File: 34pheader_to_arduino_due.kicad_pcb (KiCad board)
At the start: 2 copper layers, 29 x 59 mm, 7 parts, among them J1 Conn_02x17_Odd_Even, J2 Conn_02x17_Odd_Even, J3 Conn_01x02_Pin, J4 Conn_01x02_Pin, J5 Conn_01x02_Pin

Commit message: Add WayWayWay text to indicate the project number should be on the back silkscreen
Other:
- board text added: "WayWayWay"
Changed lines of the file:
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@@
   (gr_rect (start 206 19) (end 235 78)
     (stroke (width 0.05) (type default)) (fill none) (layer "Edge.Cuts"))
+  (gr_text "WayWayWay" (at 209.55 25.4 90) (layer "B.SilkS")
+    (effects (font (size 1 1) (thickness 0.15)) (justify left bottom mirror))
+  )
   (segment (start 231.14 63.5) (end 229.87 64.77) (width 0.25) (layer "B.Cu") (net 1))
   (segment (start 226.06 64.77) (end 218.44 72.39) (width 0.25) (layer "B.Cu") (net 1))

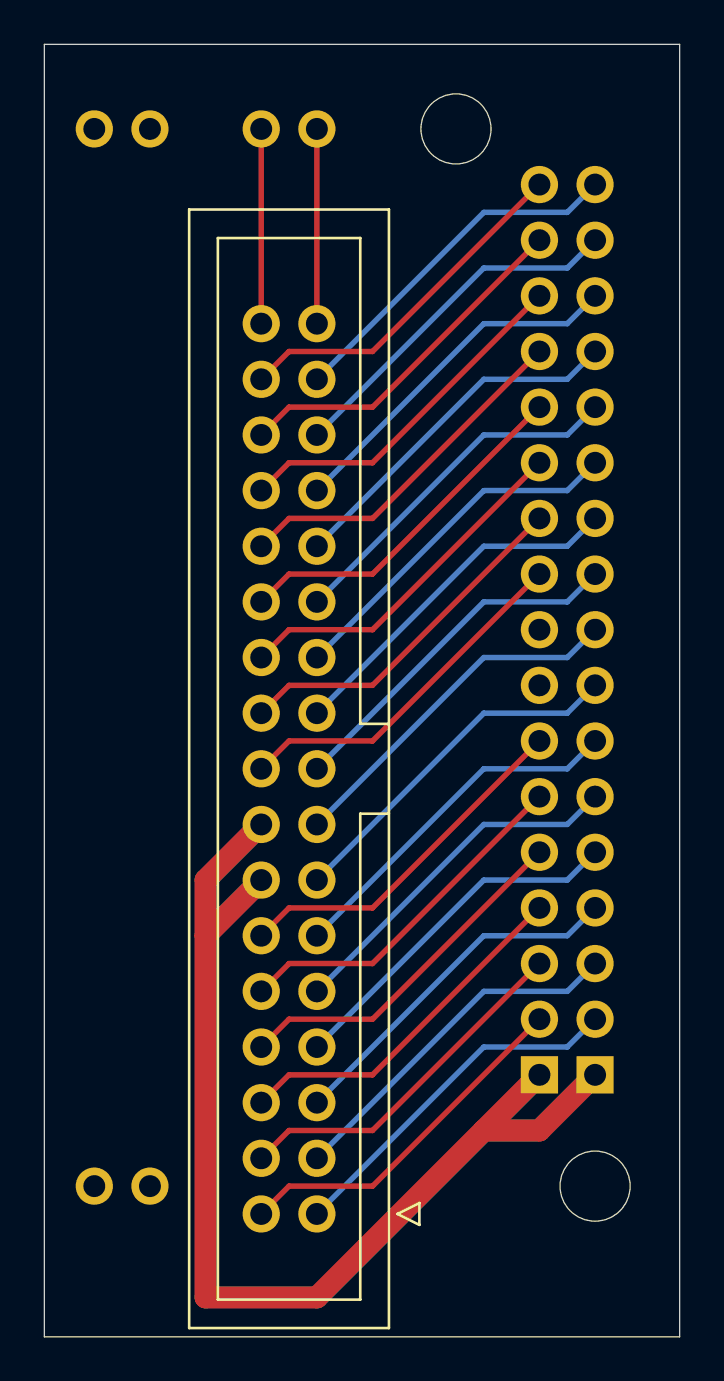
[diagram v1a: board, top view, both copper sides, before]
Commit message: Add pin numbers on silk screen layer
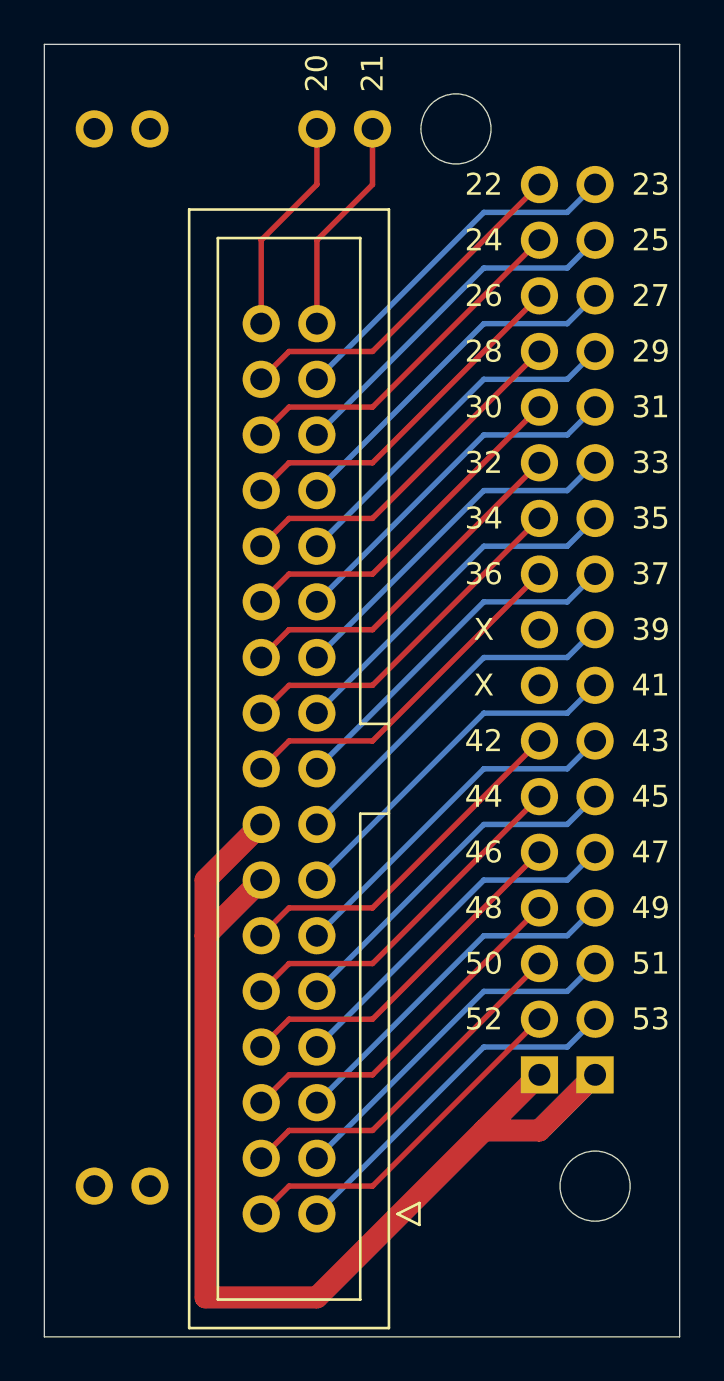
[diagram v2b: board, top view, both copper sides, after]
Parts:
- moved J3 2.54 mm to (221.0, 22.9)
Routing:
- net Net-(J1-Pin_34): track 8.89 -> 9.94 mm
- net Net-(J1-Pin_33): track 8.89 -> 9.94 mm
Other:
- board text added: "20"
- board text added: "21"
- board text added: "22"
- board text added: "23"
- board text added: "24"
- board text added: "25"
- board text added: "26"
- board text added: "27"
- board text added: "28"
- board text added: "29"
- board text added: "30"
- board text added: "31"
- board text added: "32"
- board text added: "33"
- board text added: "34"
- board text added: "35"
- board text added: "36"
- board text added: "37"
- board text added: "39"
- board text added: "41"
- board text added: "42"
- board text added: "43"
- board text added: "44"
- board text added: "45"
- board text added: "46"
- board text added: "47"
- board text added: "48"
- board text added: "49"
- board text added: "50"
- board text added: "51"
- board text added: "52"
- board text added: "53"
- board text added: "X"
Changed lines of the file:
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@@
   )
   (footprint "Connector_PinHeader_2.54mm:PinHeader_1x02_P2.54mm_Vertical" (layer "B.Cu")
-    (at 218.44 22.86 90)
+    (at 220.98 22.86 90)
     (descr "Through hole straight pin header, 1x02, 2.54mm pitch, single row")
     (tags "Through hole pin header THT 1x02 2.54mm single row")
@@
   (gr_text "WayWayWay" (at 209.55 25.4 90) (layer "B.SilkS")
     (effects (font (size 1 1) (thickness 0.15)) (justify left bottom mirror))
+  )
+  (gr_text "31" (at 233.68 35.56) (layer "F.SilkS")
+    (effects (font (size 1 1) (thickness 0.15)))
+  )
+  (gr_text "X" (at 226.06 45.72) (layer "F.SilkS")
+    (effects (font (size 1 1) (thickness 0.15)))
+  )
+  (gr_text "48" (at 226.06 58.42) (layer "F.SilkS")
+    (effects (font (size 1 1) (thickness 0.15)))
+  )
+  (gr_text "45" (at 233.68 53.34) (layer "F.SilkS")
+    (effects (font (size 1 1) (thickness 0.15)))
+  )
+  (gr_text "50" (at 226.06 60.96) (layer "F.SilkS")
+    (effects (font (size 1 1) (thickness 0.15)))
+  )
+  (gr_text "42" (at 226.06 50.8) (layer "F.SilkS")
+    (effects (font (size 1 1) (thickness 0.15)))
+  )
+  (gr_text "49" (at 233.68 58.42) (layer "F.SilkS")
+    (effects (font (size 1 1) (thickness 0.15)))
+  )
+  (gr_text "36" (at 226.06 43.18) (layer "F.SilkS")
+    (effects (font (size 1 1) (thickness 0.15)))
+  )
+  (gr_text "24" (at 226.06 27.94) (layer "F.SilkS")
+    (effects (font (size 1 1) (thickness 0.15)))
+  )
+  (gr_text "32" (at 226.06 38.1) (layer "F.SilkS")
+    (effects (font (size 1 1) (thickness 0.15)))
+  )
+  (gr_text "20" (at 218.44 20.32 90) (layer "F.SilkS")
+    (effects (font (size 1 1) (thickness 0.15)))
+  )
+  (gr_text "51" (at 233.68 60.96) (layer "F.SilkS")
+    (effects (font (size 1 1) (thickness 0.15)))
+  )
+  (gr_text "29" (at 233.68 33.02) (layer "F.SilkS")
+    (effects (font (size 1 1) (thickness 0.15)))
+  )
+  (gr_text "52" (at 226.06 63.5) (layer "F.SilkS")
+    (effects (font (size 1 1) (thickness 0.15)))
+  )
+  (gr_text "23" (at 233.68 25.4) (layer "F.SilkS")
+    (effects (font (size 1 1) (thickness 0.15)))
+  )
+  (gr_text "34" (at 226.06 40.64) (layer "F.SilkS")
+    (effects (font (size 1 1) (thickness 0.15)))
+  )
+  (gr_text "33" (at 233.68 38.1) (layer "F.SilkS")
+    (effects (font (size 1 1) (thickness 0.15)))
+  )
+  (gr_text "39" (at 233.68 45.72) (layer "F.SilkS")
+    (effects (font (size 1 1) (thickness 0.15)))
+  )
+  (gr_text "37" (at 233.68 43.18) (layer "F.SilkS")
+    (effects (font (size 1 1) (thickness 0.15)))
+  )
+  (gr_text "30" (at 226.06 35.56) (layer "F.SilkS")
+    (effects (font (size 1 1) (thickness 0.15)))
+  )
+  (gr_text "53" (at 233.68 63.5) (layer "F.SilkS")
+    (effects (font (size 1 1) (thickness 0.15)))
+  )
+  (gr_text "25" (at 233.68 27.94) (layer "F.SilkS")
+    (effects (font (size 1 1) (thickness 0.15)))
+  )
+  (gr_text "43" (at 233.68 50.8) (layer "F.SilkS")
+    (effects (font (size 1 1) (thickness 0.15)))
+  )
+  (gr_text "41" (at 233.68 48.26) (layer "F.SilkS")
+    (effects (font (size 1 1) (thickness 0.15)))
+  )
+  (gr_text "26" (at 226.06 30.48) (layer "F.SilkS")
+    (effects (font (size 1 1) (thickness 0.15)))
+  )
+  (gr_text "27" (at 233.68 30.48) (layer "F.SilkS")
+    (effects (font (size 1 1) (thickness 0.15)))
+  )
+  (gr_text "35" (at 233.68 40.64) (layer "F.SilkS")
+    (effects (font (size 1 1) (thickness 0.15)))
+  )
+  (gr_text "28" (at 226.06 33.02) (layer "F.SilkS")
+    (effects (font (size 1 1) (thickness 0.15)))
+  )
+  (gr_text "22" (at 226.06 25.4) (layer "F.SilkS")
+    (effects (font (size 1 1) (thickness 0.15)))
+  )
+  (gr_text "47" (at 233.68 55.88) (layer "F.SilkS")
+    (effects (font (size 1 1) (thickness 0.15)))
+  )
+  (gr_text "44" (at 226.06 53.34) (layer "F.SilkS")
+    (effects (font (size 1 1) (thickness 0.15)))
+  )
+  (gr_text "46" (at 226.06 55.88) (layer "F.SilkS")
+    (effects (font (size 1 1) (thickness 0.15)))
+  )
+  (gr_text "X" (at 226.06 48.26) (layer "F.SilkS")
+    (effects (font (size 1 1) (thickness 0.15)))
+  )
+  (gr_text "21" (at 220.98 20.32 90) (layer "F.SilkS")
+    (effects (font (size 1 1) (thickness 0.15)))
   )
   (segment (start 231.14 63.5) (end 229.87 64.77) (width 0.25) (layer "B.Cu") (net 1))
@@
   (segment (start 220.98 33.02) (end 228.6 25.4) (width 0.25) (layer "F.Cu") (net 30))
   (segment (start 217.17 33.02) (end 220.98 33.02) (width 0.25) (layer "F.Cu") (net 30))
-  (segment (start 218.44 31.75) (end 218.44 22.86) (width 0.25) (layer "F.Cu") (net 31))
-  (segment (start 215.9 31.75) (end 215.9 22.86) (width 0.25) (layer "F.Cu") (net 32))
+  (segment (start 220.98 25.4) (end 220.98 22.86) (width 0.25) (layer "F.Cu") (net 31))
+  (segment (start 218.44 27.94) (end 220.98 25.4) (width 0.25) (layer "F.Cu") (net 31))
+  (segment (start 218.44 31.75) (end 218.44 27.94) (width 0.25) (layer "F.Cu") (net 31))
+  (segment (start 215.9 27.94) (end 215.9 31.75) (width 0.25) (layer "F.Cu") (net 32))
+  (segment (start 218.44 22.86) (end 218.44 25.4) (width 0.25) (layer "F.Cu") (net 32))
+  (segment (start 218.44 25.4) (end 215.9 27.94) (width 0.25) (layer "F.Cu") (net 32))
   (segment (start 218.44 76.2) (end 213.36 76.2) (width 1) (layer "F.Cu") (net 39))
   (segment (start 213.36 59.69) (end 213.36 57.15) (width 1) (layer "F.Cu") (net 39))

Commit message: Add GND label
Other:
- board text added: "GND"
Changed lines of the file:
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@@
     )
   )
+  (gr_rect (start 227.33 64.77) (end 232.41 67.31)
+    (stroke (width 0.12) (type default)) (fill none) (layer "F.SilkS"))
   (gr_rect (start 206 19) (end 235 78)
     (stroke (width 0.05) (type default)) (fill none) (layer "Edge.Cuts"))
@@
     (effects (font (size 1 1) (thickness 0.15)))
   )
+  (gr_text "GND" (at 225.425 66.04) (layer "F.SilkS")
+    (effects (font (size 1 1) (thickness 0.15)))
+  )

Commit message: Ensure pinout is correct
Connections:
- J1 pad 16: Net-(J1-Pin_14) -> Net-(J1-Pin_16)
- J1 pad 22: Net-(J1-Pin_22) -> Net-(J1-Pin_20)
- J2 pad 1: Net-(J1-Pin_14) -> Net-(J1-Pin_20)
- J2 pad 16: unconnected-(J2-Pin_16-Pad16) -> Net-(J1-Pin_14)
- J2 pad 18: unconnected-(J2-Pin_18-Pad18) -> Net-(J1-Pin_16)
- J2 pad 2: Net-(J1-Pin_14) -> Net-(J1-Pin_20)
- J2 pad 22: Net-(J1-Pin_20) -> unconnected-(J2-Pin_22-Pad22)
- J2 pad 24: Net-(J1-Pin_22) -> unconnected-(J2-Pin_24-Pad24)
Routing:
- net Net-(J1-Pin_20): track 16.4 -> 118.9 mm
- net Net-(J1-Pin_14): track 103.6 -> 16.4 mm
- net Net-(J1-Pin_22): track 16.4 -> 0.00 mm
- net Net-(J1-Pin_16): track 0.00 -> 16.4 mm
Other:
- board text added: "38"
- board text added: "40"
- board text removed: "32"
- board text removed: "34"
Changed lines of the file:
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@@
   (net 18 "Net-(J1-Pin_20)")
   (net 19 "Net-(J1-Pin_21)")
-  (net 20 "Net-(J1-Pin_22)")
+  (net 20 "Net-(J1-Pin_16)")
   (net 21 "Net-(J1-Pin_23)")
   (net 22 "Net-(J1-Pin_24)")
@@
   (net 31 "Net-(J1-Pin_33)")
   (net 32 "Net-(J1-Pin_34)")
-  (net 33 "unconnected-(J2-Pin_16-Pad16)")
-  (net 34 "unconnected-(J2-Pin_18-Pad18)")
+  (net 33 "unconnected-(J2-Pin_22-Pad22)")
+  (net 34 "unconnected-(J2-Pin_24-Pad24)")
   (net 35 "unconnected-(J4-Pin_1-Pad1)")
   (net 36 "unconnected-(J4-Pin_2-Pad2)")
@@
       (net 14 "Net-(J1-Pin_15)") (pinfunction "Pin_15") (pintype "passive"))
     (pad "16" thru_hole circle (at 2.54 17.78 180) (size 1.7 1.7) (drill 1) (layers "*.Cu" "*.Mask")
-      (net 39 "Net-(J1-Pin_14)") (pinfunction "Pin_16") (pintype "passive"))
+      (net 20 "Net-(J1-Pin_16)") (pinfunction "Pin_16") (pintype "passive"))
     (pad "17" thru_hole circle (at 0 20.32 180) (size 1.7 1.7) (drill 1) (layers "*.Cu" "*.Mask")
       (net 15 "Net-(J1-Pin_17)") (pinfunction "Pin_17") (pintype "passive"))
@@
       (net 19 "Net-(J1-Pin_21)") (pinfunction "Pin_21") (pintype "passive"))
     (pad "22" thru_hole circle (at 2.54 25.4 180) (size 1.7 1.7) (drill 1) (layers "*.Cu" "*.Mask")
-      (net 20 "Net-(J1-Pin_22)") (pinfunction "Pin_22") (pintype "passive"))
+      (net 18 "Net-(J1-Pin_20)") (pinfunction "Pin_22") (pintype "passive"))
     (pad "23" thru_hole circle (at 0 27.94 180) (size 1.7 1.7) (drill 1) (layers "*.Cu" "*.Mask")
       (net 21 "Net-(J1-Pin_23)") (pinfunction "Pin_23") (pintype "passive"))
@@
       (stroke (width 0.1) (type solid)) (layer "B.Fab"))
     (pad "1" thru_hole rect (at 2.54 0) (size 1.7 1.7) (drill 1) (layers "*.Cu" "*.Mask")
-      (net 39 "Net-(J1-Pin_14)") (pinfunction "Pin_1") (pintype "passive"))
+      (net 18 "Net-(J1-Pin_20)") (pinfunction "Pin_1") (pintype "passive"))
     (pad "2" thru_hole rect (at 0 0) (size 1.7 1.7) (drill 1) (layers "*.Cu" "*.Mask")
-      (net 39 "Net-(J1-Pin_14)") (pinfunction "Pin_2") (pintype "passive"))
+      (net 18 "Net-(J1-Pin_20)") (pinfunction "Pin_2") (pintype "passive"))
     (pad "3" thru_hole oval (at 2.54 -2.54) (size 1.7 1.7) (drill 1) (layers "*.Cu" "*.Mask")
       (net 1 "Net-(J1-Pin_1)") (pinfunction "Pin_3") (pintype "passive"))
@@
       (net 13 "Net-(J1-Pin_13)") (pinfunction "Pin_15") (pintype "passive"))
     (pad "16" thru_hole oval (at 0 -17.78) (size 1.7 1.7) (drill 1) (layers "*.Cu" "*.Mask")
-      (net 33 "unconnected-(J2-Pin_16-Pad16)") (pinfunction "Pin_16") (pintype "passive+no_connect"))
+      (net 39 "Net-(J1-Pin_14)") (pinfunction "Pin_16") (pintype "passive"))
     (pad "17" thru_hole oval (at 2.54 -20.32) (size 1.7 1.7) (drill 1) (layers "*.Cu" "*.Mask")
       (net 14 "Net-(J1-Pin_15)") (pinfunction "Pin_17") (pintype "passive"))
     (pad "18" thru_hole oval (at 0 -20.32) (size 1.7 1.7) (drill 1) (layers "*.Cu" "*.Mask")
-      (net 34 "unconnected-(J2-Pin_18-Pad18)") (pinfunction "Pin_18") (pintype "passive+no_connect"))
+      (net 20 "Net-(J1-Pin_16)") (pinfunction "Pin_18") (pintype "passive"))
     (pad "19" thru_hole oval (at 2.54 -22.86) (size 1.7 1.7) (drill 1) (layers "*.Cu" "*.Mask")
       (net 15 "Net-(J1-Pin_17)") (pinfunction "Pin_19") (pintype "passive"))
@@
       (net 17 "Net-(J1-Pin_19)") (pinfunction "Pin_21") (pintype "passive"))
     (pad "22" thru_hole oval (at 0 -25.4) (size 1.7 1.7) (drill 1) (layers "*.Cu" "*.Mask")
-      (net 18 "Net-(J1-Pin_20)") (pinfunction "Pin_22") (pintype "passive"))
+      (net 33 "unconnected-(J2-Pin_22-Pad22)") (pinfunction "Pin_22") (pintype "passive+no_connect"))
     (pad "23" thru_hole oval (at 2.54 -27.94) (size 1.7 1.7) (drill 1) (layers "*.Cu" "*.Mask")
       (net 19 "Net-(J1-Pin_21)") (pinfunction "Pin_23") (pintype "passive"))
     (pad "24" thru_hole oval (at 0 -27.94) (size 1.7 1.7) (drill 1) (layers "*.Cu" "*.Mask")
-      (net 20 "Net-(J1-Pin_22)") (pinfunction "Pin_24") (pintype "passive"))
+      (net 34 "unconnected-(J2-Pin_24-Pad24)") (pinfunction "Pin_24") (pintype "passive+no_connect"))
     (pad "25" thru_hole oval (at 2.54 -30.48) (size 1.7 1.7) (drill 1) (layers "*.Cu" "*.Mask")
       (net 21 "Net-(J1-Pin_23)") (pinfunction "Pin_25") (pintype "passive"))
@@
     (effects (font (size 1 1) (thickness 0.15)))
   )
-  (gr_text "X" (at 226.06 45.72) (layer "F.SilkS")
+  (gr_text "38" (at 226.06 45.72) (layer "F.SilkS")
     (effects (font (size 1 1) (thickness 0.15)))
   )
@@
     (effects (font (size 1 1) (thickness 0.15)))
   )
-  (gr_text "32" (at 226.06 38.1) (layer "F.SilkS")
+  (gr_text "X" (at 226.06 38.1) (layer "F.SilkS")
     (effects (font (size 1 1) (thickness 0.15)))
   )
@@
     (effects (font (size 1 1) (thickness 0.15)))
   )
-  (gr_text "34" (at 226.06 40.64) (layer "F.SilkS")
+  (gr_text "X" (at 226.06 40.64) (layer "F.SilkS")
     (effects (font (size 1 1) (thickness 0.15)))
   )
@@
     (effects (font (size 1 1) (thickness 0.15)))
   )
-  (gr_text "X" (at 226.06 48.26) (layer "F.SilkS")
+  (gr_text "40" (at 226.06 48.26) (layer "F.SilkS")
     (effects (font (size 1 1) (thickness 0.15)))
   )
@@
   (segment (start 226.06 41.91) (end 218.44 49.53) (width 0.25) (layer "B.Cu") (net 17))
   (segment (start 229.87 41.91) (end 226.06 41.91) (width 0.25) (layer "B.Cu") (net 17))
-  (segment (start 217.17 48.26) (end 220.98 48.26) (width 0.25) (layer "F.Cu") (net 18))
-  (segment (start 220.98 48.26) (end 228.6 40.64) (width 0.25) (layer "F.Cu") (net 18))
-  (segment (start 215.9 49.53) (end 217.17 48.26) (width 0.25) (layer "F.Cu") (net 18))
+  (segment (start 226.06 68.58) (end 218.44 76.2) (width 1) (layer "F.Cu") (net 18))
+  (segment (start 213.36 52.07) (end 213.36 49.53) (width 1) (layer "F.Cu") (net 18))
+  (segment (start 218.44 76.2) (end 213.36 76.2) (width 1) (layer "F.Cu") (net 18))
+  (segment (start 213.36 49.53) (end 215.9 46.99) (width 1) (layer "F.Cu") (net 18))
+  (segment (start 213.36 52.07) (end 215.9 49.53) (width 1) (layer "F.Cu") (net 18))
+  (segment (start 226.06 68.58) (end 228.6 68.58) (width 1) (layer "F.Cu") (net 18))
+  (segment (start 213.36 76.2) (end 213.36 52.07) (width 1) (layer "F.Cu") (net 18))
+  (segment (start 228.6 66.04) (end 226.06 68.58) (width 1) (layer "F.Cu") (net 18))
+  (segment (start 228.6 68.58) (end 231.14 66.04) (width 1) (layer "F.Cu") (net 18))
+  (segment (start 228.6 68.58) (end 226.06 68.58) (width 1) (layer "B.Cu") (net 18))
+  (segment (start 213.36 52.07) (end 215.9 49.53) (width 1) (layer "B.Cu") (net 18))
+  (segment (start 231.14 66.04) (end 228.6 68.58) (width 1) (layer "B.Cu") (net 18))
+  (segment (start 226.06 68.58) (end 218.44 76.2) (width 1) (layer "B.Cu") (net 18))
+  (segment (start 228.6 66.04) (end 226.06 68.58) (width 1) (layer "B.Cu") (net 18))
+  (segment (start 213.36 49.53) (end 215.9 46.99) (width 1) (layer "B.Cu") (net 18))
+  (segment (start 213.36 52.07) (end 213.36 49.53) (width 1) (layer "B.Cu") (net 18))
+  (segment (start 218.44 76.2) (end 213.36 76.2) (width 1) (layer "B.Cu") (net 18))
+  (segment (start 213.36 76.2) (end 213.36 52.07) (width 1) (layer "B.Cu") (net 18))
   (segment (start 231.14 38.1) (end 229.87 39.37) (width 0.25) (layer "B.Cu") (net 19))
   (segment (start 229.87 39.37) (end 226.06 39.37) (width 0.25) (layer "B.Cu") (net 19))
   (segment (start 226.06 39.37) (end 218.44 46.99) (width 0.25) (layer "B.Cu") (net 19))
-  (segment (start 217.17 45.72) (end 220.98 45.72) (width 0.25) (layer "F.Cu") (net 20))
-  (segment (start 220.98 45.72) (end 228.6 38.1) (width 0.25) (layer "F.Cu") (net 20))
-  (segment (start 215.9 46.99) (end 217.17 45.72) (width 0.25) (layer "F.Cu") (net 20))
+  (segment (start 220.98 53.34) (end 228.6 45.72) (width 0.25) (layer "F.Cu") (net 20))
+  (segment (start 217.17 53.34) (end 220.98 53.34) (width 0.25) (layer "F.Cu") (net 20))
+  (segment (start 215.9 54.61) (end 217.17 53.34) (width 0.25) (layer "F.Cu") (net 20))
   (segment (start 226.06 36.83) (end 218.44 44.45) (width 0.25) (layer "B.Cu") (net 21))
   (segment (start 229.87 36.83) (end 226.06 36.83) (width 0.25) (layer "B.Cu") (net 21))
@@
   (segment (start 218.44 22.86) (end 218.44 25.4) (width 0.25) (layer "F.Cu") (net 32))
   (segment (start 218.44 25.4) (end 215.9 27.94) (width 0.25) (layer "F.Cu") (net 32))
-  (segment (start 218.44 76.2) (end 213.36 76.2) (width 1) (layer "F.Cu") (net 39))
-  (segment (start 213.36 59.69) (end 213.36 57.15) (width 1) (layer "F.Cu") (net 39))
-  (segment (start 213.36 76.2) (end 213.36 59.69) (width 1) (layer "F.Cu") (net 39))
-  (segment (start 226.06 68.58) (end 228.6 68.58) (width 1) (layer "F.Cu") (net 39))
-  (segment (start 226.06 68.58) (end 218.44 76.2) (width 1) (layer "F.Cu") (net 39))
-  (segment (start 213.36 57.15) (end 215.9 54.61) (width 1) (layer "F.Cu") (net 39))
-  (segment (start 215.9 57.15) (end 213.36 59.69) (width 1) (layer "F.Cu") (net 39))
-  (segment (start 228.6 66.04) (end 226.06 68.58) (width 1) (layer "F.Cu") (net 39))
-  (segment (start 228.6 68.58) (end 231.14 66.04) (width 1) (layer "F.Cu") (net 39))
-  (segment (start 228.6 68.58) (end 226.06 68.58) (width 1) (layer "B.Cu") (net 39))
-  (segment (start 231.14 66.04) (end 228.6 68.58) (width 1) (layer "B.Cu") (net 39))
-  (segment (start 218.44 76.2) (end 213.36 76.2) (width 1) (layer "B.Cu") (net 39))
-  (segment (start 228.6 66.04) (end 226.06 68.58) (width 1) (layer "B.Cu") (net 39))
-  (segment (start 226.06 68.58) (end 218.44 76.2) (width 1) (layer "B.Cu") (net 39))
-  (segment (start 215.9 57.15) (end 213.36 59.69) (width 1) (layer "B.Cu") (net 39))
-  (segment (start 213.36 76.2) (end 213.36 57.15) (width 1) (layer "B.Cu") (net 39))
-  (segment (start 213.36 57.15) (end 215.9 54.61) (width 1) (layer "B.Cu") (net 39))
+  (segment (start 217.17 55.88) (end 220.98 55.88) (width 0.25) (layer "F.Cu") (net 39))
+  (segment (start 220.98 55.88) (end 228.6 48.26) (width 0.25) (layer "F.Cu") (net 39))
+  (segment (start 215.9 57.15) (end 217.17 55.88) (width 0.25) (layer "F.Cu") (net 39))
 )
